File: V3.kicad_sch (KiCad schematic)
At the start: 104 parts, among them IC1 TPS62840DLCR","TPS62840DLCR, J1 Conn_01x04, J2 Conn_01x04, J3 FFC2B28-24-G, J6 Conn_01x02, J7 Conn_01x02, Q1 FDN304P","FDN304P, Q2 FDN304P","FDN304P, Q3 FDN304P","FDN304P, Q4 FDN304P","FDN304P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

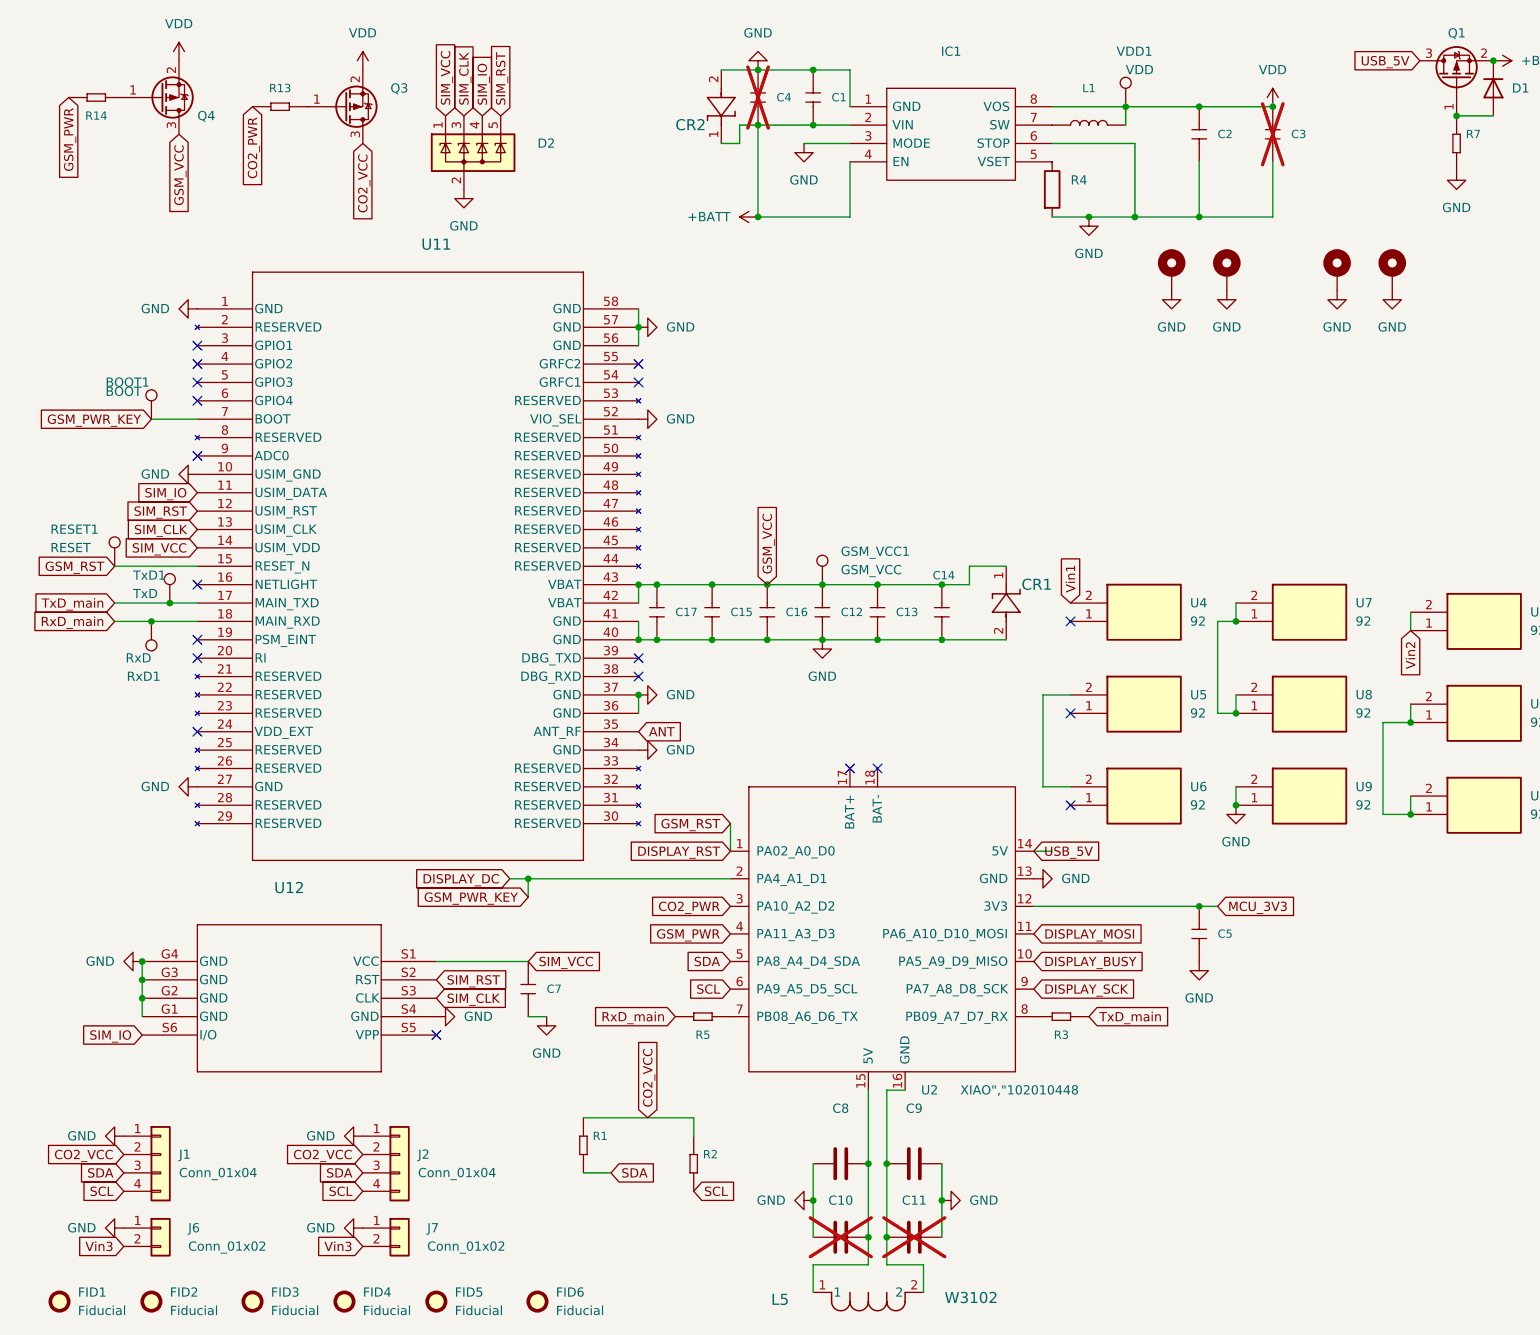
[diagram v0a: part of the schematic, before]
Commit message: add resisors to sim card, move TVS diode, add 3rd i2c header
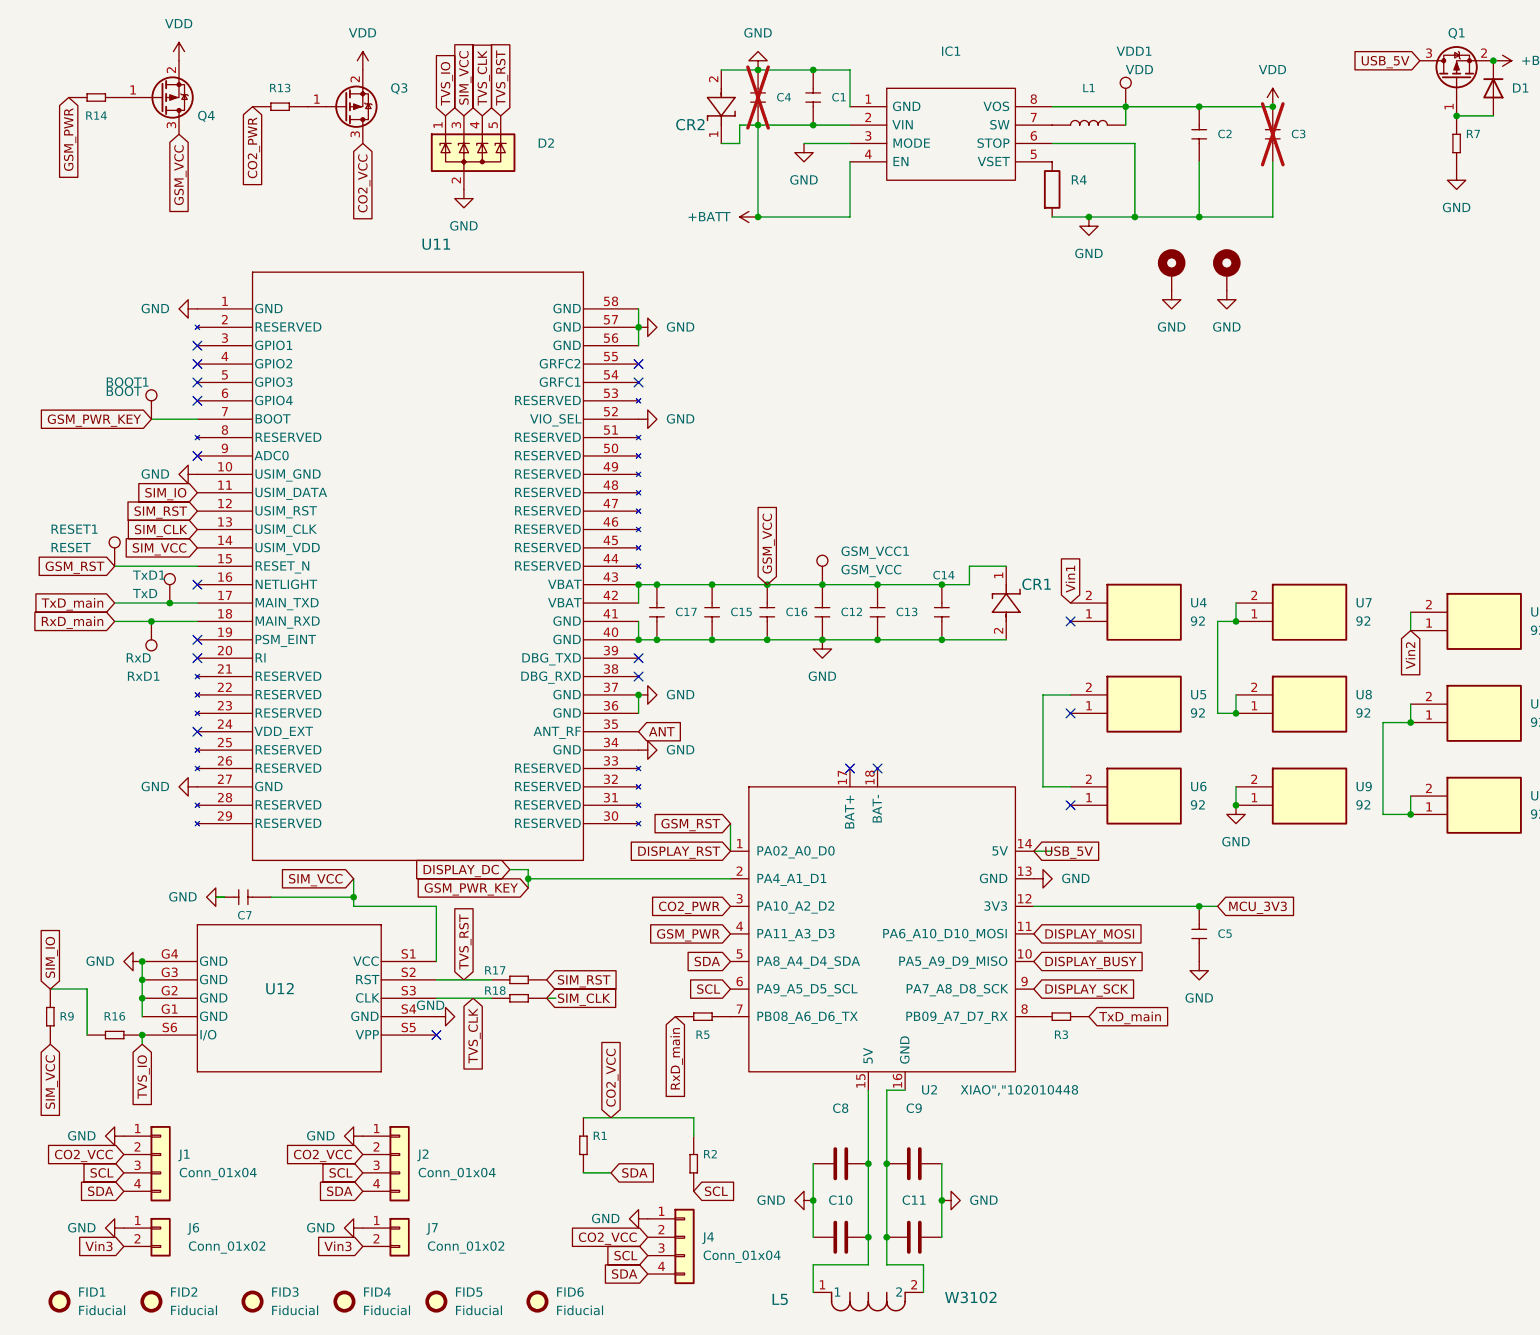
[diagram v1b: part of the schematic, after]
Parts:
- removed H3, H8: MountingHole_Pad_MP, MountingHole:MountingHole_2.7mm_M2.5_ISO14580_Pad, symbol Mechanical:MountingHole_Pad_MP
- added J4: Conn_01x04, Connector_PinSocket_2.54mm:PinSocket_1x04_P2.54mm_Vertical, symbol Connector_Generic:Conn_01x04
- added R16, R17, R18: 22R","22R, kicad_mod:R0603, symbol OPL_Resistor:SMD-RES-10K-5%-1_10W_0603_
- added R9: 10K","RC0603JR-0710KL, kicad_mod:R0603, symbol OPL_Resistor:SMD-RES-10K-5%-1_10W_0603_
- C10, C11: value ~ -> 3.6pF","CBR06C369B5GAC; now fitted
- C5, C7: footprint OPL_Capacitor:C0805 -> kicad_mod:C0805
- C8, C9: value 335pF","GCM1885C2A331JA16D -> 51pF","06031U510GAT2A
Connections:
- net CO2_VCC: now also J4.2 (Pin_2)
- net GND: now also J4.1 (Pin_1)
- net SCL: now also J1.3 (Pin_3), J2.3 (Pin_3), J4.3 (Pin_3); no longer J1.4 (Pin_4), J2.4 (Pin_4)
- net SDA: now also J1.4 (Pin_4), J2.4 (Pin_4), J4.4 (Pin_4); no longer J1.3 (Pin_3), J2.3 (Pin_3)
- net SIM_CLK: now also R18.1; no longer D2.3 (K), U12.S3 (CLK)
- net SIM_IO: now also R16.2, R9.2; no longer D2.4 (K), U12.S6 (I/O)
- net SIM_RST: now also R17.1; no longer D2.5 (K), U12.S2 (RST)
- net SIM_VCC: now also D2.3 (K), R9.1; no longer D2.1 (K)
- new net TVS_CLK: D2.4 (K), R18.2, U12.S3 (CLK)
- new net TVS_IO: D2.1 (K), R16.1, U12.S6 (I/O)
- new net TVS_RST: D2.5 (K), R17.2, U12.S2 (RST)
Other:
- moved on the sheet: C7

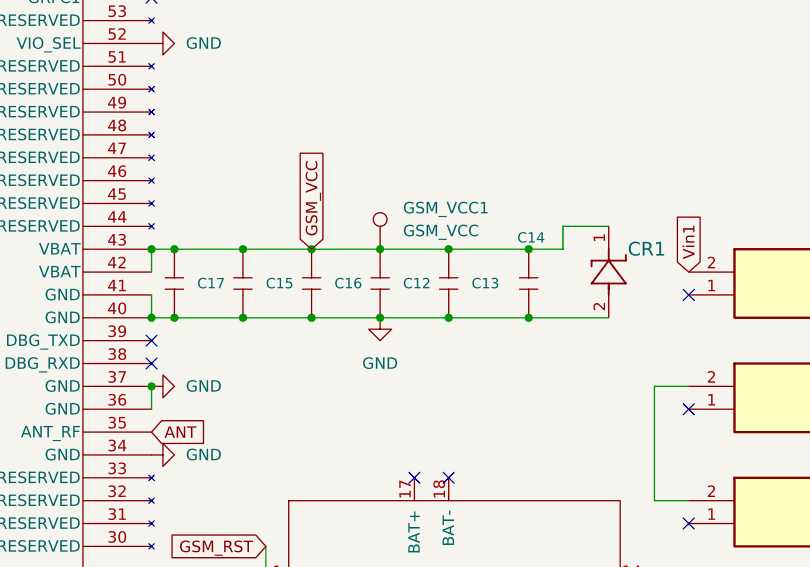
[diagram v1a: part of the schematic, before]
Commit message: add resistors for sim card. Move componets from sticky pads, make extra room for sim card holder
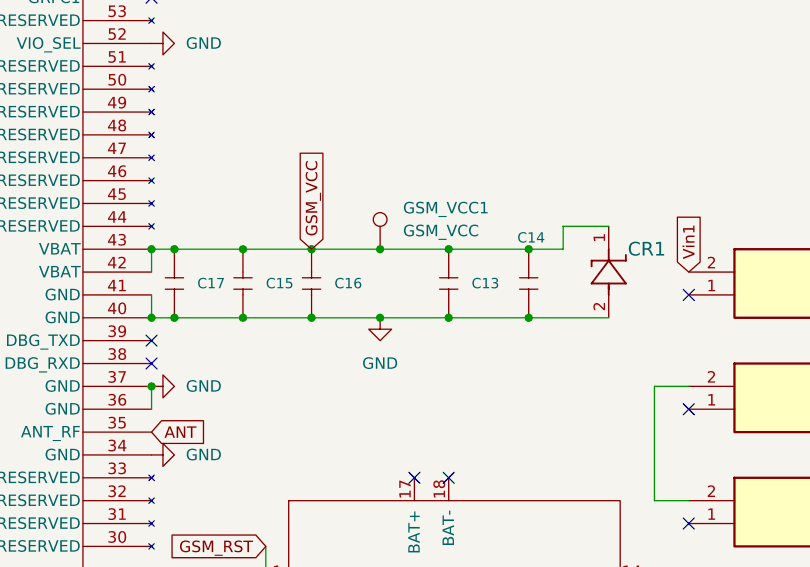
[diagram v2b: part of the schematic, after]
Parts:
- removed C12: 10uF","EMK212BJ106KG-T, kicad_mod:C0805, symbol OPL_Capacitor:CERAMIC-1UF-25V-10%-X7R_0603_
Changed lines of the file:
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@@
-	)
-	(symbol
-		(lib_id "OPL_Capacitor:CERAMIC-1UF-25V-10%-X7R_0603_")
-		(at 120.65 99.06 270)
-		(unit 1)
-		(exclude_from_sim no)
-		(in_bom yes)
-		(on_board yes)
-		(dnp no)
-		(property "Reference" "C12"
-			(at 123.19 99.06 90)
-			(effects
-				(font
-					(size 1.143 1.143)
-				)
-				(justify left)
-			)
-		)
-		(property "Value" "10uF\",\"EMK212BJ106KG-T"
-			(at 124.46 101.6 90)
-			(effects
-				(font
-					(size 1.143 1.143)
-				)
-				(hide yes)
-			)
-		)
-		(property "Footprint" "kicad_mod:C0805"
-			(at 120.65 99.06 0)
-			(effects
-				(font
-					(size 1.27 1.27)
-				)
-				(hide yes)
-			)
-		)
-		(property "Datasheet" ""
-			(at 120.65 99.06 0)
-			(effects
-				(font
-					(size 1.27 1.27)
-				)
-				(hide yes)
-			)
-		)
-		(property "Description" ""
-			(at 120.65 99.06 0)
-			(effects
-				(font
-					(size 1.27 1.27)
-				)
-				(hide yes)
-			)
-		)
-		(property "MPN" "EMK212BJ106KG-T"
-			(at 124.46 99.822 0)
-			(effects
-				(font
-					(size 0.508 0.508)
-				)
-				(hide yes)
-			)
-		)
-		(property "SKU" "302010139"
-			(at 124.46 99.822 0)
-			(effects
-				(font
-					(size 0.508 0.508)
-				)
-				(hide yes)
-			)
-		)
-		(pin "1"
-		)
-		(pin "2"
-		)
-		(instances
-			(project "Toms air quality"
-				(path "/bb9ed05e-0f43-4915-900f-41a4b6c0b434"
-					(reference "C12")
-					(unit 1)
-				)
-			)
-		)
 	)
 	(symbol

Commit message: change OR ring to diodes
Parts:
- removed Q1, Q2, Q5, Q7: FDN304P","FDN304P, Package_TO_SOT_SMD:SOT-23, symbol Transistor_FET:FDN340P
- removed R10, R6, R7, R8: 100K","RC0603JR-07100KL, kicad_mod:R0603, symbol OPL_Resistor:SMD-RES-10K-5%-1_10W_0603_
- C10, C11: now in the parts list
- J1, J2, J4, J6, J7, U10, U13, U14, U15, U16, U17, U4, U5, U6, U7, U8, U9: now left out of the parts list
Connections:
- net USB_5V: now also D1.2 (A)
- net Vin1: now also D3.2 (A)
- net Vin2: now also D4.2 (A); no longer U10.1
- net Vin3: now also D5.2 (A)
- no-connect marks 29 -> 30
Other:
- moved on the sheet: D1, D3, D4, D5, D6, Q6, R11

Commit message: replace reverse polarity mosfets with diodes
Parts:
- added D10: NSR0520V2","NSR0520V2, Diode_SMD:D_SOD-523, symbol Diode:1N4148WT
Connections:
- net MCU_3V3: now also D10.1 (K)
- net VDD: now also D10.2 (A)
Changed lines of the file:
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@@
 		)
 	)
+	(global_label "MCU_3V3"
+		(shape input)
+		(at 271.78 34.29 0)
+		(fields_autoplaced yes)
+		(effects
+			(font
+				(size 1.27 1.27)
+			)
+			(justify left)
+		)
+		(property "Intersheetrefs" "${INTERSHEET_REFS}"
+			(at 283.2923 34.29 0)
+			(effects
+				(font
+					(size 1.27 1.27)
+				)
+				(justify left)
+				(hide yes)
+			)
+		)
+	)
 	(global_label "DISPLAY_SCK"
 		(shape input)
@@
 	)
 	(symbol
+		(lib_id "Diode:1N4148WT")
+		(at 267.97 34.29 180)
+		(unit 1)
+		(exclude_from_sim no)
+		(in_bom no)
+		(on_board yes)
+		(dnp yes)
+		(fields_autoplaced yes)
+		(property "Reference" "D10"
+			(at 267.97 30.48 0)
+			(effects
+				(font
+					(size 1.27 1.27)
+				)
+			)
+		)
+		(property "Value" "NSR0520V2\",\"NSR0520V2"
+			(at 267.97 38.1 0)
+			(effects
+				(font
+					(size 1.27 1.27)
+				)
+				(hide yes)
+			)
+		)
+		(property "Footprint" "Diode_SMD:D_SOD-523"
+			(at 267.97 29.845 0)
+			(effects
+				(font
+					(size 1.27 1.27)
+				)
+				(hide yes)
+			)
+		)
+		(property "Datasheet" ""
+			(at 267.97 34.29 0)
+			(effects
+				(font
+					(size 1.27 1.27)
+				)
+				(hide yes)
+			)
+		)
+		(property "Description" "Diode, SOD-523"
+			(at 267.97 34.29 0)
+			(effects
+				(font
+					(size 1.27 1.27)
+				)
+				(hide yes)
+			)
+		)
+		(property "Sim.Device" "D"
+			(at 267.97 34.29 0)
+			(effects
+				(font
+					(size 1.27 1.27)
+				)
+				(hide yes)
+			)
+		)
+		(property "Sim.Pins" "1=K 2=A"
+			(at 267.97 34.29 0)
+			(effects
+				(font
+					(size 1.27 1.27)
+				)
+				(hide yes)
+			)
+		)
+		(pin "1"
+		)
+		(pin "2"
+		)
+		(instances
+			(project "V3"
+				(path "/bb9ed05e-0f43-4915-900f-41a4b6c0b434"
+					(reference "D10")
+					(unit 1)
+				)
+			)
+		)
+	)
+	(symbol
 		(lib_id "92:92")
 		(at 177.8 97.79 0)
@@
 					(unit 1)
 				)
+			)
+		)
+	)
+	(symbol
+		(lib_id "power:VDD")
+		(at 264.16 34.29 90)
+		(unit 1)
+		(exclude_from_sim no)
+		(in_bom yes)
+		(on_board yes)
+		(dnp no)
+		(fields_autoplaced yes)
+		(property "Reference" "#PWR02"
+			(at 267.97 34.29 0)
+			(effects
+				(font
+					(size 1.27 1.27)
+				)
+				(hide yes)
+			)
+		)
+		(property "Value" "VDD"
+			(at 260.35 34.29 90)
+			(effects
+				(font
+					(size 1.27 1.27)
+				)
+				(justify left)
+			)
+		)
+		(property "Footprint" ""
+			(at 264.16 34.29 0)
+			(effects
+				(font
+					(size 1.27 1.27)
+				)
+				(hide yes)
+			)
+		)
+		(property "Datasheet" ""
+			(at 264.16 34.29 0)
+			(effects
+				(font
+					(size 1.27 1.27)
+				)
+				(hide yes)
+			)
+		)
+		(property "Description" ""
+			(at 264.16 34.29 0)
+			(effects
+				(font
+					(size 1.27 1.27)
+				)
+				(hide yes)
+			)
+		)
+		(pin "1"
+		)
+		(instances
+			(project "V3"
+				(path "/bb9ed05e-0f43-4915-900f-41a4b6c0b434"
+					(reference "#PWR02")
+					(unit 1)
+				)

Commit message: revision to review with ideal diode oring
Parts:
- removed Q6: FDN304P","FDN304P, Package_TO_SOT_SMD:SOT-23, symbol Transistor_FET:FDN340P
- removed R11: 100K","RC0603JR-07100KL, kicad_mod:R0603, symbol OPL_Resistor:SMD-RES-10K-5%-1_10W_0603_
- added C12, C18, C6: 1uF",CC0603KRX5R7BB105, kicad_mod:C0603, symbol Device:C
- added R6, R7, R8: 10K","RC0603JR-0710KL, kicad_mod:R0603, symbol OPL_Resistor:SMD-RES-10K-5%-1_10W_0603_
- added U1, U18, U3: LM66100DCK, Package_TO_SOT_SMD:SOT-363_SC-70-6, symbol Power_Management:LM66100DCK
- D3, D4: now not fitted; now left out of the parts list
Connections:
- net +BATT: now also D6.1 (K), R6.1, R7.1, U18.6 (VOUT), U3.6 (VOUT)
- net GND: now also C12.2, C18.1, C6.1, U1.2 (GND), U1.5 (ST), U18.2 (GND), U18.5 (ST), U3.2 (GND), U3.5 (ST)
- net MCU_3V3: now also R8.1, U1.6 (VOUT); no longer D6.1 (K)
- net VDD: now also C12.1, U1.1 (VIN)
- net Vin1: now also C6.2, U3.1 (VIN)
- net Vin2: now also C18.2, U18.1 (VIN)
- net at D6.2 (A): now also J7.2 (Pin_2)
- net Vin3: no longer names the net of D5.2 (A), J6.2 (Pin_2)
- net Vin3: no longer J7.2 (Pin_2)
- new net: R6.2, U3.3 (~{CE})
- new net: R8.2, U1.3 (~{CE})
- new net: R7.2, U18.3 (~{CE})
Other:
- moved on the sheet: D1, D10, D5
